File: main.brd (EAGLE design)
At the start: 86 x 70 mm, 29 parts, among them IC1 SN754410, IC2 7805T, T1 BPX81, T2 BPX81, T3 BPX81, T4 BPX81

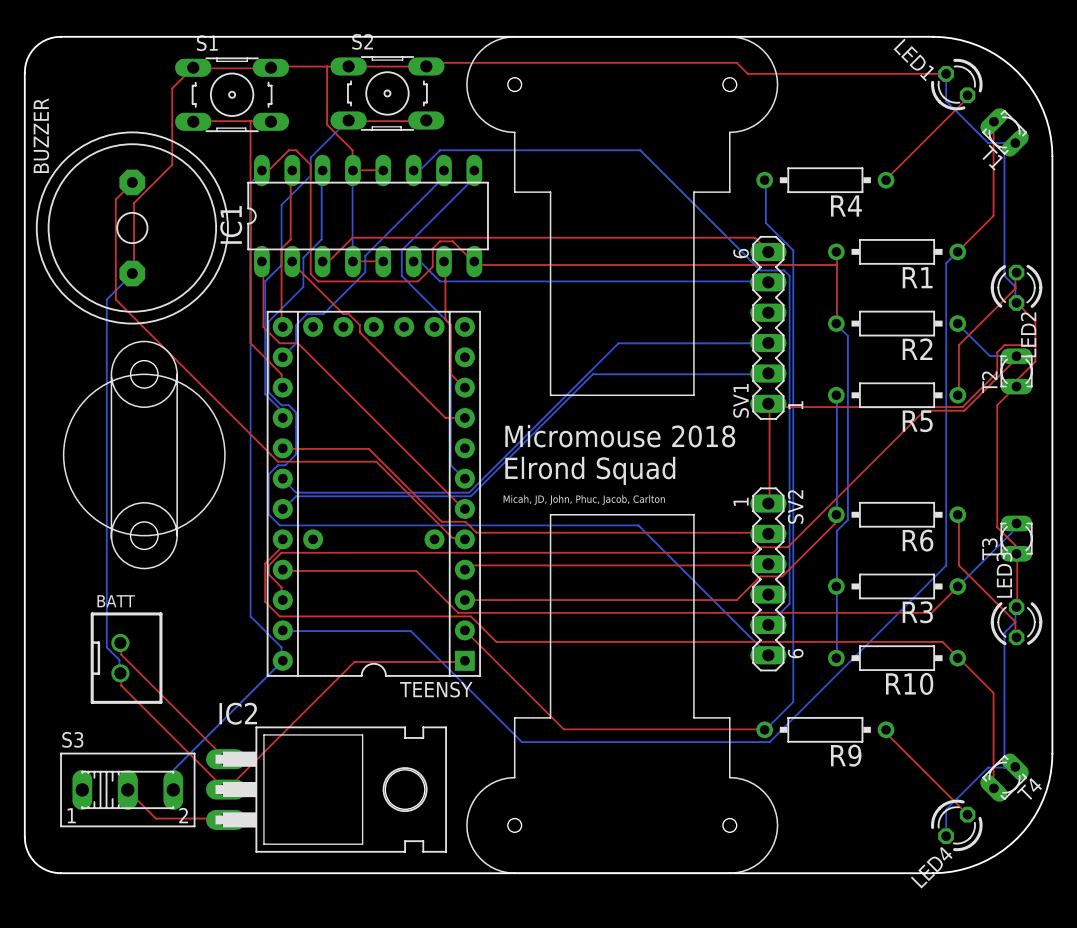
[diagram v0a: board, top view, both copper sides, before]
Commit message: Updated drill hole size and wiring
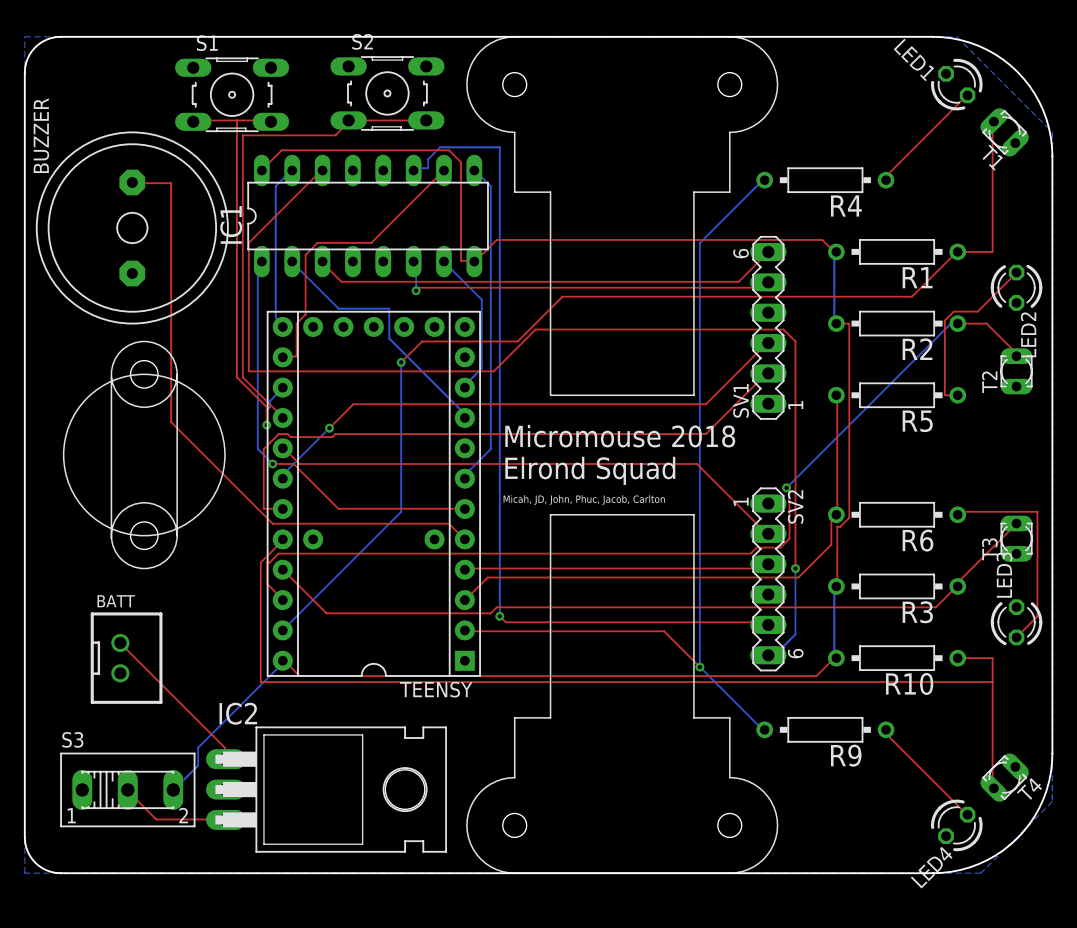
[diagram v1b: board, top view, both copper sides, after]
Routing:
- net GND: track 287.8 -> 0.00 mm
- net M2A: track 79.9 -> 94.5 mm, vias 0 -> 1
- net T1: track 104.3 -> 90.8 mm, vias 0 -> 1
- net T4: track 78.0 -> 87.8 mm
- net S1: track 30.0 -> 36.8 mm, vias 0 -> 1
- net M1E: track 28.7 -> 35.2 mm, vias 0 -> 1
- net ENC1B: track 45.3 -> 51.6 mm
- net S2: track 35.0 -> 41.0 mm
- net N$7: track 12.3 -> 18.0 mm
- net L1: track 76.6 -> 71.6 mm, vias 0 -> 1
- net BZ: track 47.9 -> 51.9 mm
- net M2B: track 66.5 -> 70.5 mm, vias 0 -> 1
- net M2E: track 30.5 -> 27.3 mm
- net +5V: track 153.9 -> 157.1 mm
- net N$6: track 12.3 -> 15.0 mm
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- added copper zone on layer 16, net GND

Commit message: Fixed broken nets on motor connectors
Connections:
- removed net VM1: SV1.4
- removed net VM2: SV2.4
- net +5V: now also SV1.4, SV2.4
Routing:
- net +5V: track 157.1 -> 169.3 mm
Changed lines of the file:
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@@
 <wire x1="69" y1="29.75" x2="68.25" y2="29" width="0.1524" layer="1"/>
 <wire x1="69" y1="46" x2="69" y2="29.75" width="0.1524" layer="1"/>
-<wire x1="67.92" y1="46" x2="69" y2="46" width="0.1524" layer="1"/>
+<wire x1="67.92" y1="46" x2="68" y2="46" width="0.1524" layer="1"/>
+<wire x1="68" y1="46" x2="69" y2="46" width="0.1524" layer="1"/>
 <wire x1="68" y1="24" x2="67.92" y2="24" width="0.1524" layer="1"/>
 <wire x1="23" y1="16.5" x2="21.75" y2="17.75" width="0.1524" layer="1"/>
@@
 <wire x1="37.75" y1="51.25" x2="37.62" y2="51.19" width="0.1524" layer="1"/>
 <wire x1="67.75" y1="52" x2="67.92" y2="52" width="0.1524" layer="1"/>
+<contactref element="SV1" pad="4"/>
+<contactref element="SV2" pad="4"/>
+<wire x1="62.23" y1="46.91" x2="67.09" y2="46.91" width="0.1524" layer="1"/>
+<wire x1="67.09" y1="46.91" x2="68" y2="46" width="0.1524" layer="1"/>
+<wire x1="62.23" y1="23.32" x2="67.32" y2="23.32" width="0.1524" layer="1"/>
+<wire x1="67.32" y1="23.32" x2="68" y2="24" width="0.1524" layer="1"/>
 </signal>
 <signal name="N$9">
@@
 <wire x1="62" y1="49.25" x2="62.23" y2="49.45" width="0.1524" layer="1"/>
 <via x="32.75" y="48.75" extent="1-16" drill="0.35"/>
-</signal>
-<signal name="VM1">
-<contactref element="SV1" pad="4"/>
 </signal>
 <signal name="M1A">
@@
 <via x="64.5" y="25.5" extent="1-16" drill="0.35"/>
 </signal>
-<signal name="VM2">
-<contactref element="SV2" pad="4"/>
-</signal>
 </signals>
